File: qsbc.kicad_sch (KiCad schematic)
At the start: 4 parts

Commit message: misc cleanup, change from usb mux to dual uart
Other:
- sheet Peripherals ports: added UART1_CTS, UART1_RTS, UART1_RXI, UART1_TXO; removed none
- sheet USB ports: added UART1_CTS, UART1_RTS, UART1_RXI, UART1_TXO; removed none

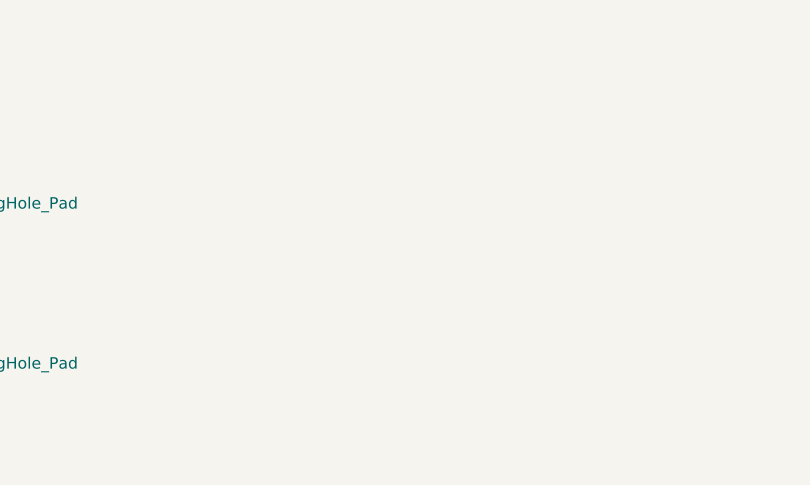
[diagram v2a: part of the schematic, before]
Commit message: add imx8mm 3d model, add FIDs
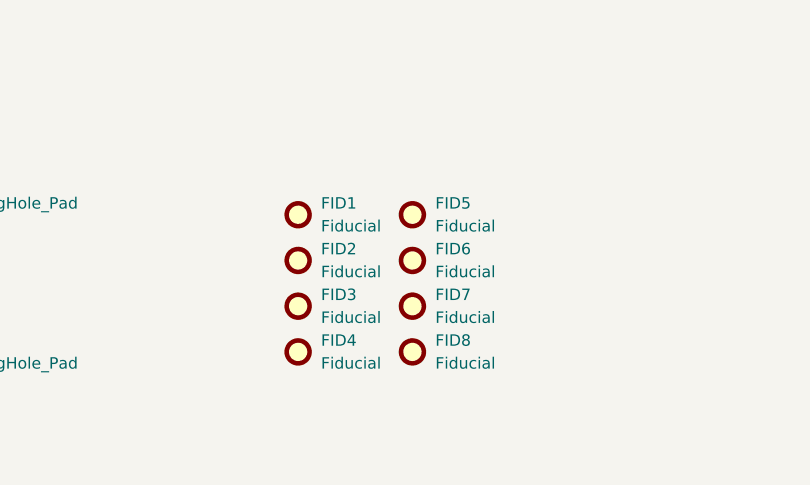
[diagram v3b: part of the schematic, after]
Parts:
- added FID1, FID2, FID3, FID4, FID5, FID6, FID7, FID8: Fiducial, Fiducial:Fiducial_0.5mm_Mask1mm, symbol Mechanical:Fiducial
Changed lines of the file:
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@@
+    )
+  )
+  (symbol (lib_id "Mechanical:Fiducial") (at 102.87 377.19 0) (unit 1)
+    (in_bom no) (on_board yes) (fields_autoplaced)
+    (property "Reference" "FID4" (id 0) (at 105.41 375.9199 0)
+      (effects (font (size 1.27 1.27)) (justify left))
+    )
+    (property "Value" "Fiducial" (id 1) (at 105.41 378.4599 0)
+      (effects (font (size 1.27 1.27)) (justify left))
+    )
+    (property "Footprint" "Fiducial:Fiducial_0.5mm_Mask1mm" (id 2) (at 102.87 377.19 0)
+      (effects (font (size 1.27 1.27)) hide)
+    )
+    (property "Datasheet" "~" (id 3) (at 102.87 377.19 0)
+      (effects (font (size 1.27 1.27)) hide)
+    )
+  )
+  (symbol (lib_id "Mechanical:Fiducial") (at 115.57 377.19 0) (unit 1)
+    (in_bom no) (on_board yes) (fields_autoplaced)
+    (property "Reference" "FID8" (id 0) (at 118.11 375.9199 0)
+      (effects (font (size 1.27 1.27)) (justify left))
+    )
+    (property "Value" "Fiducial" (id 1) (at 118.11 378.4599 0)
+      (effects (font (size 1.27 1.27)) (justify left))
+    )
+    (property "Footprint" "Fiducial:Fiducial_0.5mm_Mask1mm" (id 2) (at 115.57 377.19 0)
+      (effects (font (size 1.27 1.27)) hide)
+    )
+    (property "Datasheet" "~" (id 3) (at 115.57 377.19 0)
+      (effects (font (size 1.27 1.27)) hide)
+    )
+  )
+  (symbol (lib_id "Mechanical:Fiducial") (at 102.87 361.95 0) (unit 1)
+    (in_bom no) (on_board yes) (fields_autoplaced)
+    (property "Reference" "FID1" (id 0) (at 105.41 360.6799 0)
+      (effects (font (size 1.27 1.27)) (justify left))
+    )
+    (property "Value" "Fiducial" (id 1) (at 105.41 363.2199 0)
+      (effects (font (size 1.27 1.27)) (justify left))
+    )
+    (property "Footprint" "Fiducial:Fiducial_0.5mm_Mask1mm" (id 2) (at 102.87 361.95 0)
+      (effects (font (size 1.27 1.27)) hide)
+    )
+    (property "Datasheet" "~" (id 3) (at 102.87 361.95 0)
+      (effects (font (size 1.27 1.27)) hide)
+    )
+  )
+  (symbol (lib_id "Mechanical:Fiducial") (at 102.87 372.11 0) (unit 1)
+    (in_bom no) (on_board yes) (fields_autoplaced)
+    (property "Reference" "FID3" (id 0) (at 105.41 370.8399 0)
+      (effects (font (size 1.27 1.27)) (justify left))
+    )
+    (property "Value" "Fiducial" (id 1) (at 105.41 373.3799 0)
+      (effects (font (size 1.27 1.27)) (justify left))
+    )
+    (property "Footprint" "Fiducial:Fiducial_0.5mm_Mask1mm" (id 2) (at 102.87 372.11 0)
+      (effects (font (size 1.27 1.27)) hide)
+    )
+    (property "Datasheet" "~" (id 3) (at 102.87 372.11 0)
+      (effects (font (size 1.27 1.27)) hide)
     )
   )
@@
     (pin "1")
   )
+  (symbol (lib_id "Mechanical:Fiducial") (at 115.57 361.95 0) (unit 1)
+    (in_bom no) (on_board yes) (fields_autoplaced)
+    (property "Reference" "FID5" (id 0) (at 118.11 360.6799 0)
+      (effects (font (size 1.27 1.27)) (justify left))
+    )
+    (property "Value" "Fiducial" (id 1) (at 118.11 363.2199 0)
+      (effects (font (size 1.27 1.27)) (justify left))
+    )
+    (property "Footprint" "Fiducial:Fiducial_0.5mm_Mask1mm" (id 2) (at 115.57 361.95 0)
+      (effects (font (size 1.27 1.27)) hide)
+    )
+    (property "Datasheet" "~" (id 3) (at 115.57 361.95 0)
+      (effects (font (size 1.27 1.27)) hide)
+    )
+  )
+  (symbol (lib_id "Mechanical:Fiducial") (at 115.57 372.11 0) (unit 1)
+    (in_bom no) (on_board yes) (fields_autoplaced)
+    (property "Reference" "FID7" (id 0) (at 118.11 370.8399 0)
+      (effects (font (size 1.27 1.27)) (justify left))
+    )
+    (property "Value" "Fiducial" (id 1) (at 118.11 373.3799 0)
+      (effects (font (size 1.27 1.27)) (justify left))
+    )
+    (property "Footprint" "Fiducial:Fiducial_0.5mm_Mask1mm" (id 2) (at 115.57 372.11 0)
+      (effects (font (size 1.27 1.27)) hide)
+    )
+    (property "Datasheet" "~" (id 3) (at 115.57 372.11 0)
+      (effects (font (size 1.27 1.27)) hide)
+    )
+  )
   (symbol (lib_id "Mechanical:MountingHole_Pad") (at 35.56 378.46 0) (unit 1)
     (in_bom yes) (on_board yes) (fields_autoplaced)
@@
     (pin "1")
   )
+  (symbol (lib_id "Mechanical:Fiducial") (at 115.57 367.03 0) (unit 1)
+    (in_bom no) (on_board yes) (fields_autoplaced)
+    (property "Reference" "FID6" (id 0) (at 118.11 365.7599 0)
+      (effects (font (size 1.27 1.27)) (justify left))
+    )
+    (property "Value" "Fiducial" (id 1) (at 118.11 368.2999 0)
+      (effects (font (size 1.27 1.27)) (justify left))
+    )
+    (property "Footprint" "Fiducial:Fiducial_0.5mm_Mask1mm" (id 2) (at 115.57 367.03 0)
+      (effects (font (size 1.27 1.27)) hide)
+    )
+    (property "Datasheet" "~" (id 3) (at 115.57 367.03 0)
+      (effects (font (size 1.27 1.27)) hide)
+    )
+  )
   (symbol (lib_id "Mechanical:MountingHole_Pad") (at 59.69 378.46 0) (unit 1)
     (in_bom yes) (on_board yes) (fields_autoplaced)
@@
     )
     (pin "1")
+  )
+  (symbol (lib_id "Mechanical:Fiducial") (at 102.87 367.03 0) (unit 1)
+    (in_bom no) (on_board yes) (fields_autoplaced)
+    (property "Reference" "FID2" (id 0) (at 105.41 365.7599 0)
+      (effects (font (size 1.27 1.27)) (justify left))
+    )
+    (property "Value" "Fiducial" (id 1) (at 105.41 368.2999 0)
+      (effects (font (size 1.27 1.27)) (justify left))
+    )
+    (property "Footprint" "Fiducial:Fiducial_0.5mm_Mask1mm" (id 2) (at 102.87 367.03 0)
+      (effects (font (size 1.27 1.27)) hide)
+    )
+    (property "Datasheet" "~" (id 3) (at 102.87 367.03 0)
+      (effects (font (size 1.27 1.27)) hide)
+    )
   )
   (sheet (at 292.1 228.6) (size 63.5 63.5) (fields_autoplaced)
@@
       (reference "D8") (unit 1) (value "LED_Yellow") (footprint "LED_SMD:LED_0603_1608Metric")
     )
+    (path "/09230357-833b-403a-95d2-80eedef32163"
+      (reference "FID1") (unit 1) (value "Fiducial") (footprint "Fiducial:Fiducial_0.5mm_Mask1mm")
+    )
+    (path "/f1799324-f651-4e44-83ab-0b97f78de4f4"
+      (reference "FID2") (unit 1) (value "Fiducial") (footprint "Fiducial:Fiducial_0.5mm_Mask1mm")
+    )
+    (path "/17894155-8c7e-4440-a30e-4a0d1592c5be"
+      (reference "FID3") (unit 1) (value "Fiducial") (footprint "Fiducial:Fiducial_0.5mm_Mask1mm")
+    )
+    (path "/046b7697-5ded-4569-bd05-bbd93396a6fb"
+      (reference "FID4") (unit 1) (value "Fiducial") (footprint "Fiducial:Fiducial_0.5mm_Mask1mm")
+    )
+    (path "/3919e58b-5bba-4e53-aea6-22a4f90da8b7"
+      (reference "FID5") (unit 1) (value "Fiducial") (footprint "Fiducial:Fiducial_0.5mm_Mask1mm")
+    )
+    (path "/7e3f9ff8-19cc-4e7d-8417-6eefbc7d8534"
+      (reference "FID6") (unit 1) (value "Fiducial") (footprint "Fiducial:Fiducial_0.5mm_Mask1mm")
+    )
+    (path "/4bca0ff9-7cab-4609-94cb-f40d90cd4b3a"
+      (reference "FID7") (unit 1) (value "Fiducial") (footprint "Fiducial:Fiducial_0.5mm_Mask1mm")
+    )
+    (path "/07b2ab06-94f7-40b2-83f0-494cfca432d8"
+      (reference "FID8") (unit 1) (value "Fiducial") (footprint "Fiducial:Fiducial_0.5mm_Mask1mm")
+    )
     (path "/73eee985-f5b2-4f65-bca7-008434fb35fe"

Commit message: Rev 1
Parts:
- removed FID1, FID2, FID3, FID4, FID5, FID6, FID7, FID8: Fiducial, Fiducial:Fiducial_0.5mm_Mask1mm, symbol Mechanical:Fiducial
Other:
- note added: "Fix for hidden power pin net names"

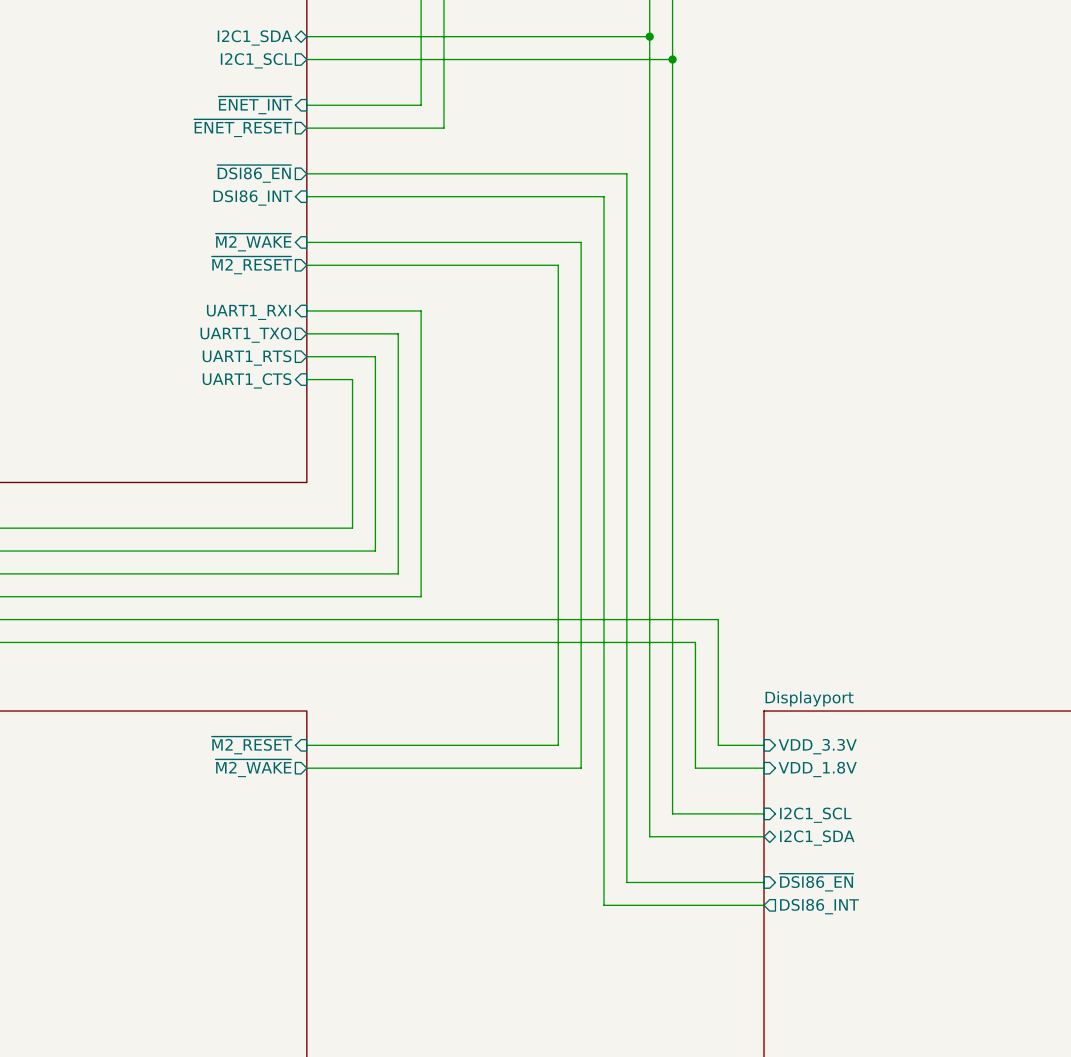
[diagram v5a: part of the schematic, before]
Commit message: dsi86: en is active high
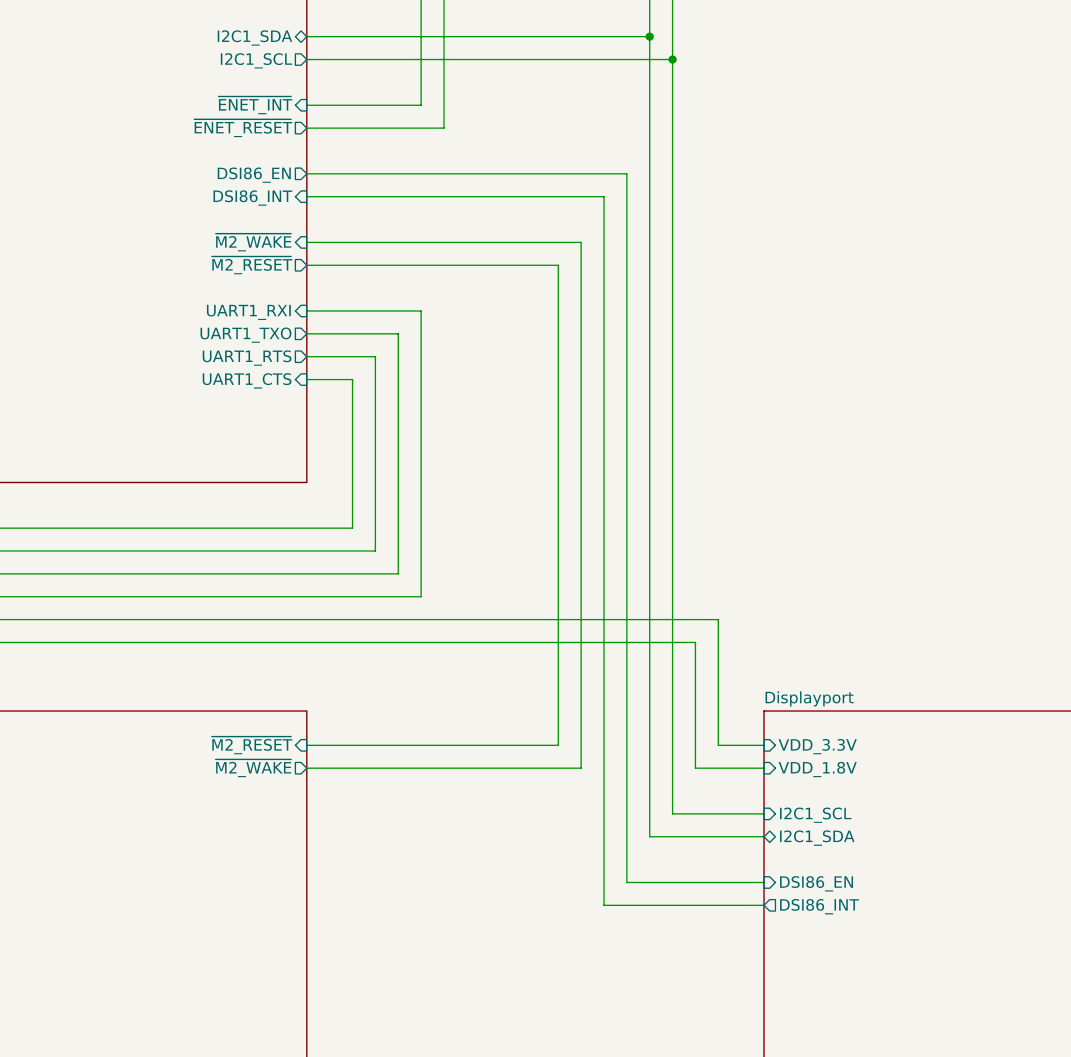
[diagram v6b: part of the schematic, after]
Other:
- sheet Displayport ports: added DSI86_EN; removed ~{DSI86_EN}
- sheet Peripherals ports: added DSI86_EN; removed ~{DSI86_EN}
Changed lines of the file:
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@@
       (effects (font (size 1.27 1.27)) (justify left))
     )
-    (pin "~{DSI86_EN}" output (at 355.6 257.81 0)
+    (pin "DSI86_EN" output (at 355.6 257.81 0)
       (effects (font (size 1.27 1.27)) (justify right))
     )
@@
       (effects (font (size 1.27 1.27)) (justify left))
     )
-    (pin "~{DSI86_EN}" input (at 406.4 336.55 180)
+    (pin "DSI86_EN" input (at 406.4 336.55 180)
       (effects (font (size 1.27 1.27)) (justify left))
     )
